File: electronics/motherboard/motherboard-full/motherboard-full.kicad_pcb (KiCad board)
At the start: 2 copper layers, 106.6 x 156.6 mm, 73 parts, among them J1 TBP02R2-381-02BE, J10 ST1W008S4AR1500, J11 MICROMOD_FUNCTION__MAIN, J12 TBP02R2-381-03BE, J13 TBP02R2-381-03BE, J14 TBP02R2-381-02BE, J2 Conn_01x04_Male, J3 USB4145-03-0230-C_REVA, J4 MICROMOD_-2222-C, J6 Conn_01x06_Female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

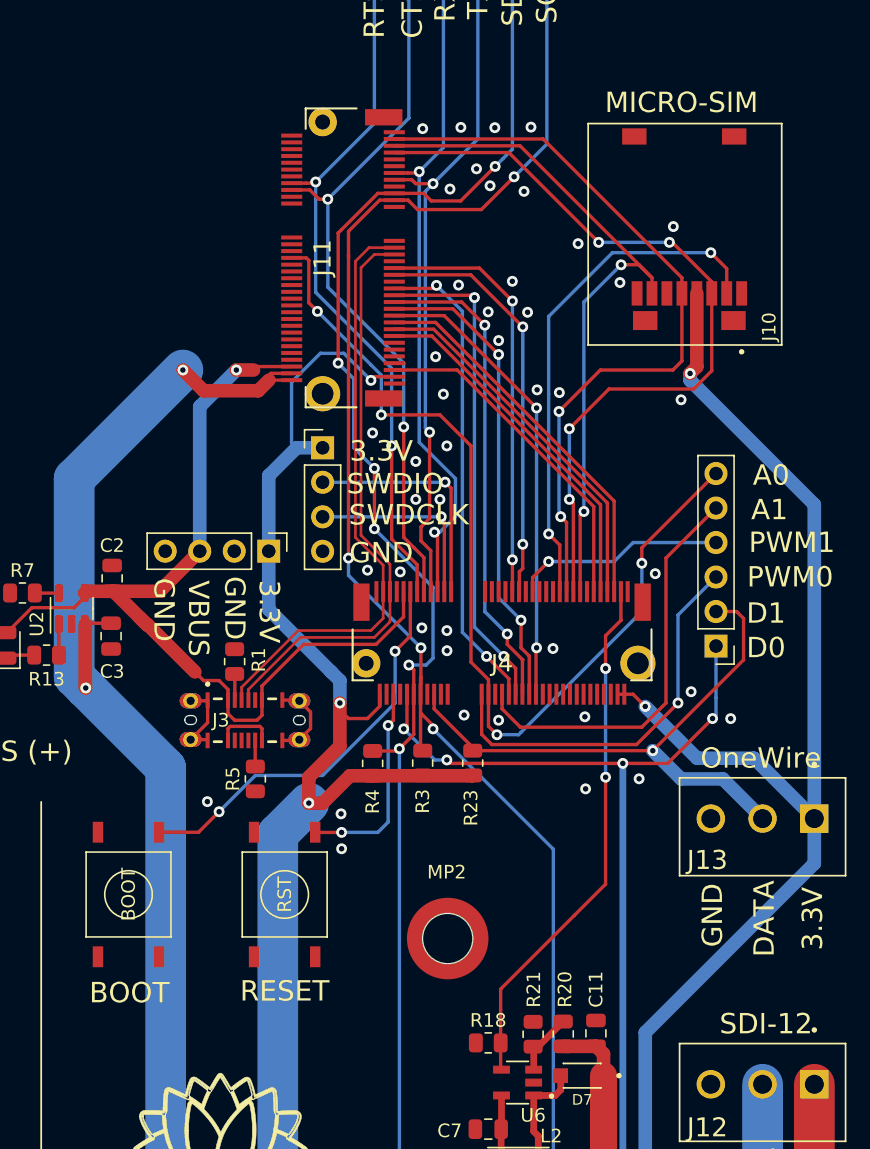
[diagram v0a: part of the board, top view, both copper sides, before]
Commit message: realign with master branch before kangaroo board is split into seperate repo
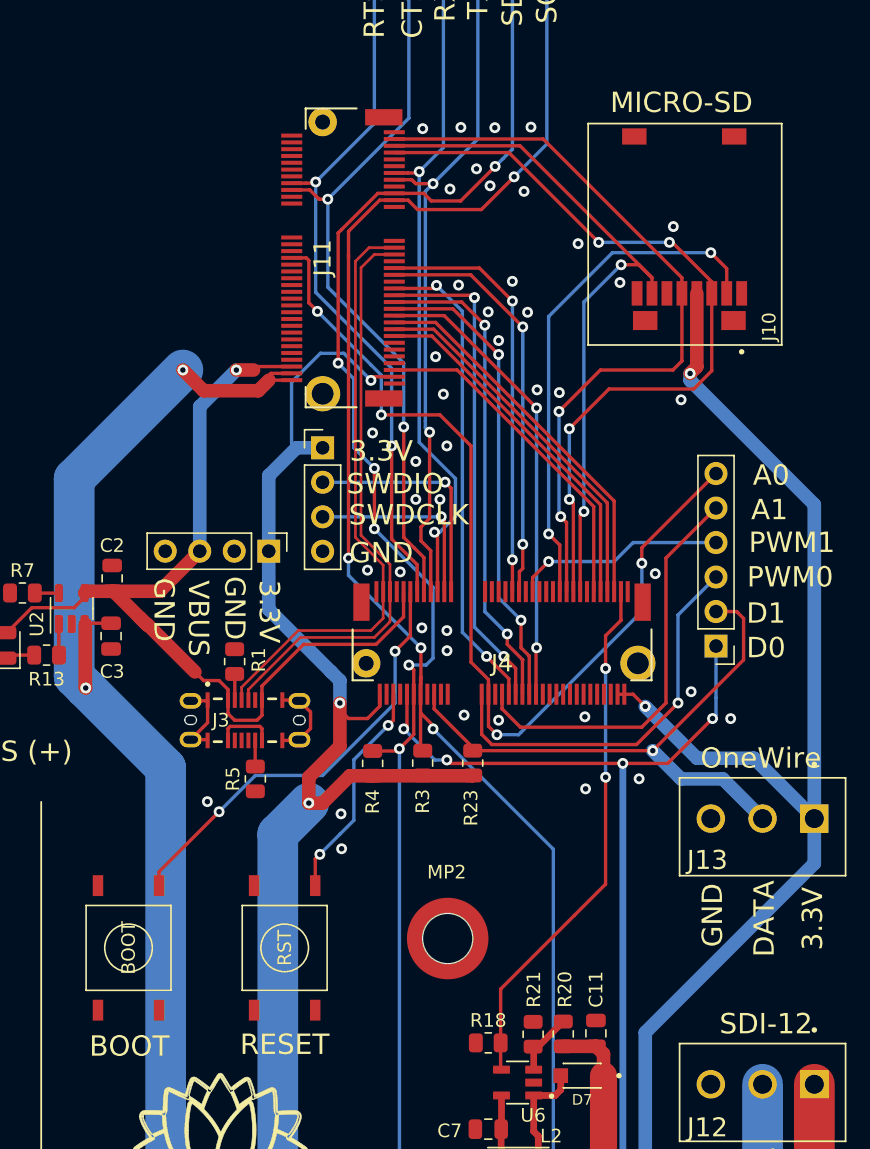
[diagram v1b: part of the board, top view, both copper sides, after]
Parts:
- moved SW1 3.93 mm to (105.4, 112.4)
- moved SW2 3.93 mm to (93.9, 112.4)
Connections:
- BT1 pad C1-: (no net) -> GND
- BT1 pad C2-: (no net) -> GND
- SW1 pad 1: unconnected-(SW1-Pad1) -> GND
- SW1 pad 2: GND -> unconnected-(SW1-Pad2)
- SW2 pad 1: unconnected-(SW2-Pad1) -> GND
- SW2 pad 2: GND -> unconnected-(SW2-Pad2)
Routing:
- net BOOT: track 30.0 -> 32.2 mm
- net RESET: track 15.3 -> 16.5 mm
- net (no net): vias 1 -> 0
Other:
- board text added: "MICRO-SD"
- board text removed: "MICRO-SIM"
